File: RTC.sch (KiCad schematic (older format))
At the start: 4 parts

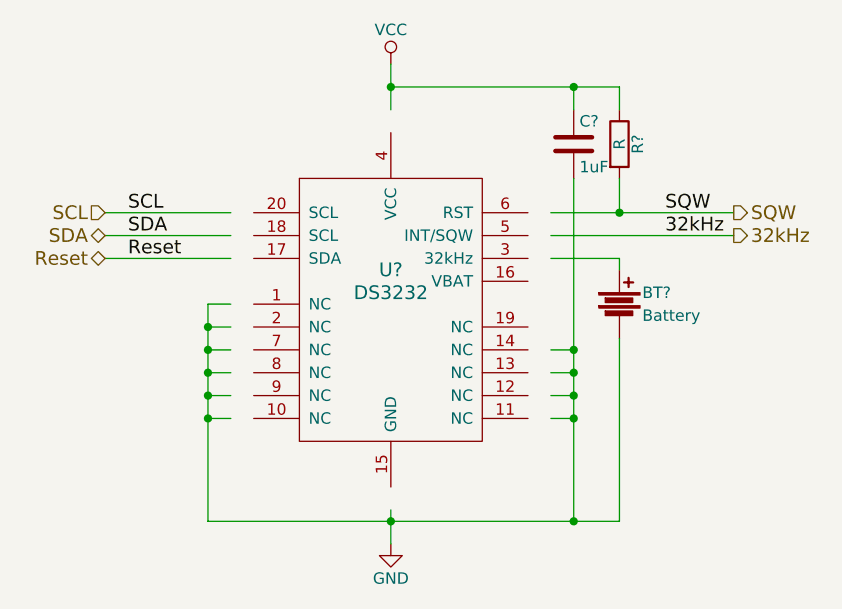
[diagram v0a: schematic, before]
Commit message: schematic and provisional layout for RTC and RS232
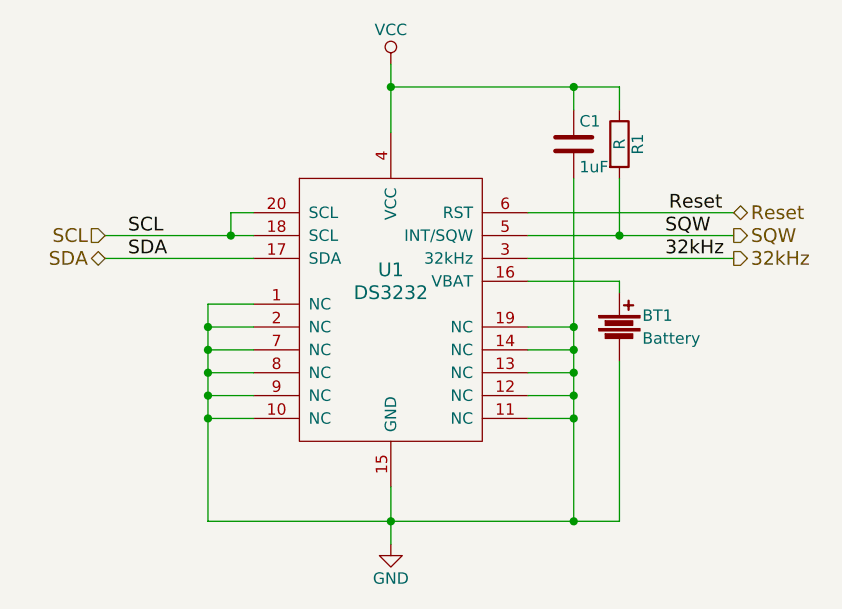
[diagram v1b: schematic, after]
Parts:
- C1: renamed from C?; footprint (none) -> Capacitors_SMD:C_1206
- R1: renamed from R?; footprint (none) -> Resistors_SMD:R_0603
- gave numbers to parts that had none: 2
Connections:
- wire segments 27 -> 30
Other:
- moved on the sheet: BT1
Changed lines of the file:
@@
 $Descr A4 11693 8268
 encoding utf-8
-Sheet 3 3
+Sheet 3 4
 Title ""
 Date ""
@@
 $EndDescr
 $Comp
-L DS3232 U?
+L DS3232 U1
 U 1 1 5559EE2D
 P 5700 3750
-F 0 "U?" H 5700 3850 60  0000 C CNN
+F 0 "U1" H 5700 3850 60  0000 C CNN
 F 1 "DS3232" H 5700 3750 60  0000 C CNN
-F 2 "" H 5700 3750 60  0000 C CNN
+F 2 "" H 4450 4350 60  0001 C CNN
 F 3 "" H 5700 3750 60  0000 C CNN
 	1    5700 3750
@@
 $EndComp
 $Comp
-L GND #PWR?
+L GND #PWR05
 U 1 1 5559EED7
 P 5700 4850
-F 0 "#PWR?" H 5700 4600 50  0001 C CNN
+F 0 "#PWR05" H 5700 4600 50  0001 C CNN
 F 1 "GND" H 5700 4700 50  0000 C CNN
 F 2 "" H 5700 4850 60  0000 C CNN
@@
 $EndComp
 $Comp
-L VCC #PWR?
+L VCC #PWR06
 U 1 1 5559EEEC
 P 5700 2750
-F 0 "#PWR?" H 5700 2600 50  0001 C CNN
+F 0 "#PWR06" H 5700 2600 50  0001 C CNN
 F 1 "VCC" H 5700 2900 50  0000 C CNN
 F 2 "" H 5700 2750 60  0000 C CNN
@@
 $EndComp
 Wire Wire Line
-	5000 3800 4900 3800
+	4900 3800 5100 3800
 Wire Wire Line
 	4900 3800 4900 4750
@@
 	4900 4750 6700 4750
 Wire Wire Line
-	5700 4700 5700 4850
+	5700 4600 5700 4850
 Connection ~ 5700 4750
 Wire Wire Line
-	5000 3900 4900 3900
+	4900 3900 5100 3900
 Connection ~ 4900 3900
 Wire Wire Line
-	5000 4000 4900 4000
+	4900 4000 5100 4000
 Connection ~ 4900 4000
 Wire Wire Line
-	5000 4100 4900 4100
+	4900 4100 5100 4100
 Connection ~ 4900 4100
 Wire Wire Line
-	5000 4200 4900 4200
+	4900 4200 5100 4200
 Connection ~ 4900 4200
 Wire Wire Line
-	5000 4300 4900 4300
+	4900 4300 5100 4300
 Connection ~ 4900 4300
 Wire Wire Line
-	6400 4000 6500 4000
+	6500 4000 6300 4000
 Wire Wire Line
 	6500 3250 6500 4750
+Connection ~ 6500 4000
 Wire Wire Line
-	6400 4100 6500 4100
-Connection ~ 6500 4100
-Wire Wire Line
-	6400 4200 6500 4200
+	6300 4200 6500 4200
 Connection ~ 6500 4200
 Wire Wire Line
-	6400 4300 6500 4300
+	6300 4300 6500 4300
 Connection ~ 6500 4300
 $Comp
-L Battery BT?
+L Battery BT1
 U 1 1 5559EFFD
-P 6700 3800
-F 0 "BT?" H 6800 3850 50  0000 L CNN
-F 1 "Battery" H 6800 3750 50  0000 L CNN
-F 2 "" V 6700 3840 60  0000 C CNN
-F 3 "" V 6700 3840 60  0000 C CNN
-	1    6700 3800
+P 6700 3900
+F 0 "BT1" H 6800 3950 50  0000 L CNN
+F 1 "Battery" H 6800 3850 50  0000 L CNN
+F 2 "" V 6700 3940 60  0001 C CNN
+F 3 "" V 6700 3940 60  0000 C CNN
+	1    6700 3900
 	1    0    0    -1
 $EndComp
 Wire Wire Line
-	6400 3600 6700 3600
+	6300 3700 6700 3700
 Wire Wire Line
-	6700 3600 6700 3650
+	6700 3700 6700 3750
 Wire Wire Line
-	6700 4750 6700 3950
+	6700 4750 6700 4050
 Connection ~ 6500 4750
 Wire Wire Line
-	6400 3500 7200 3500
+	6300 3600 7200 3600
 Wire Wire Line
-	6400 3400 7200 3400
+	6300 3500 7200 3500
 $Comp
-L R R?
+L R R1
 U 1 1 5559F0B5
 P 6700 3100
-F 0 "R?" V 6780 3100 50  0000 C CNN
+F 0 "R1" V 6780 3100 50  0000 C CNN
 F 1 "R" V 6700 3100 50  0000 C CNN
-F 2 "" V 6630 3100 30  0000 C CNN
+F 2 "Resistors_SMD:R_0603" V 6630 3100 30  0001 C CNN
 F 3 "" H 6700 3100 30  0000 C CNN
 	1    6700 3100
@@
 $EndComp
 Wire Wire Line
-	6700 3400 6700 3250
-Connection ~ 6700 3400
+	6700 3500 6700 3250
+Connection ~ 6700 3500
 Wire Wire Line
 	5700 2850 6700 2850
@@
 	6700 2850 6700 2950
 Wire Wire Line
-	5700 2750 5700 2950
+	5700 2750 5700 3050
 Connection ~ 5700 2850
 $Comp
-L C C?
+L C C1
 U 1 1 5559F187
 P 6500 3100
-F 0 "C?" H 6525 3200 50  0000 L CNN
+F 0 "C1" H 6525 3200 50  0000 L CNN
 F 1 "1uF" H 6525 3000 50  0000 L CNN
-F 2 "" H 6538 2950 30  0000 C CNN
+F 2 "Capacitors_SMD:C_1206" H 6538 2950 30  0001 C CNN
 F 3 "" H 6500 3100 60  0000 C CNN
 	1    6500 3100
@@
 $EndComp
 Wire Wire Line
-	6500 2950 6500 2850
+	6500 2850 6500 2950
 Connection ~ 6500 2850
-Connection ~ 6500 4000
-Text Label 6900 3400 0    60   ~ 0
+Text Label 6900 3500 0    60   ~ 0
 SQW
-Text Label 6900 3500 0    60   ~ 0
+Text Label 6900 3600 0    60   ~ 0
 32kHz
 Wire Wire Line
-	5000 3600 4450 3600
+	6300 3400 7200 3400
 Wire Wire Line
-	5000 3500 4450 3500
+	4450 3600 5100 3600
 Wire Wire Line
-	5000 3400 4450 3400
+	4450 3500 5100 3500
+Text Label 7150 3400 2    60   ~ 0
+Reset
 Text Label 4550 3600 0    60   ~ 0
+SDA
+Text Label 4550 3500 0    60   ~ 0
+SCL
+Text HLabel 7200 3500 2    60   Output ~ 0
+SQW
+Text HLabel 7200 3600 2    60   Output ~ 0
+32kHz
+Text HLabel 4450 3500 0    60   Input ~ 0
+SCL
+Text HLabel 4450 3600 0    60   BiDi ~ 0
+SDA
+Text HLabel 7200 3400 2    60   BiDi ~ 0
 Reset
-Text Label 4550 3500 0    60   ~ 0
-SDA
-Text Label 4550 3400 0    60   ~ 0
-SCL
-Text HLabel 7200 3400 2    60   Output ~ 0
-SQW
-Text HLabel 7200 3500 2    60   Output ~ 0
-32kHz
-Text HLabel 4450 3400 0    60   Input ~ 0
-SCL
-Text HLabel 4450 3500 0    60   BiDi ~ 0
-SDA
-Text HLabel 4450 3600 0    60   BiDi ~ 0
-Reset
+Wire Wire Line
+	6500 4100 6300 4100
+Connection ~ 6500 4100
+Wire Wire Line
+	6300 3900 6500 3900
+Connection ~ 6500 3900
+Wire Wire Line
+	5100 3400 5000 3400
+Wire Wire Line
+	5000 3400 5000 3500
+Connection ~ 5000 3500
 $EndSCHEMATC
